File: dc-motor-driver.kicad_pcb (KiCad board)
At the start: 2 copper layers, 33 x 39.5 mm, 29 parts, among them J1 Conn_01x03, J10 Right, J11 RL, J12 RR, J2 MPU, J3 BAT, J4 Conn_01x03, J5 Power, J6 Left, J7 Conn_01x03, J8 FL, J9 FR, Q1 IRF7303, Q2 IRF7303

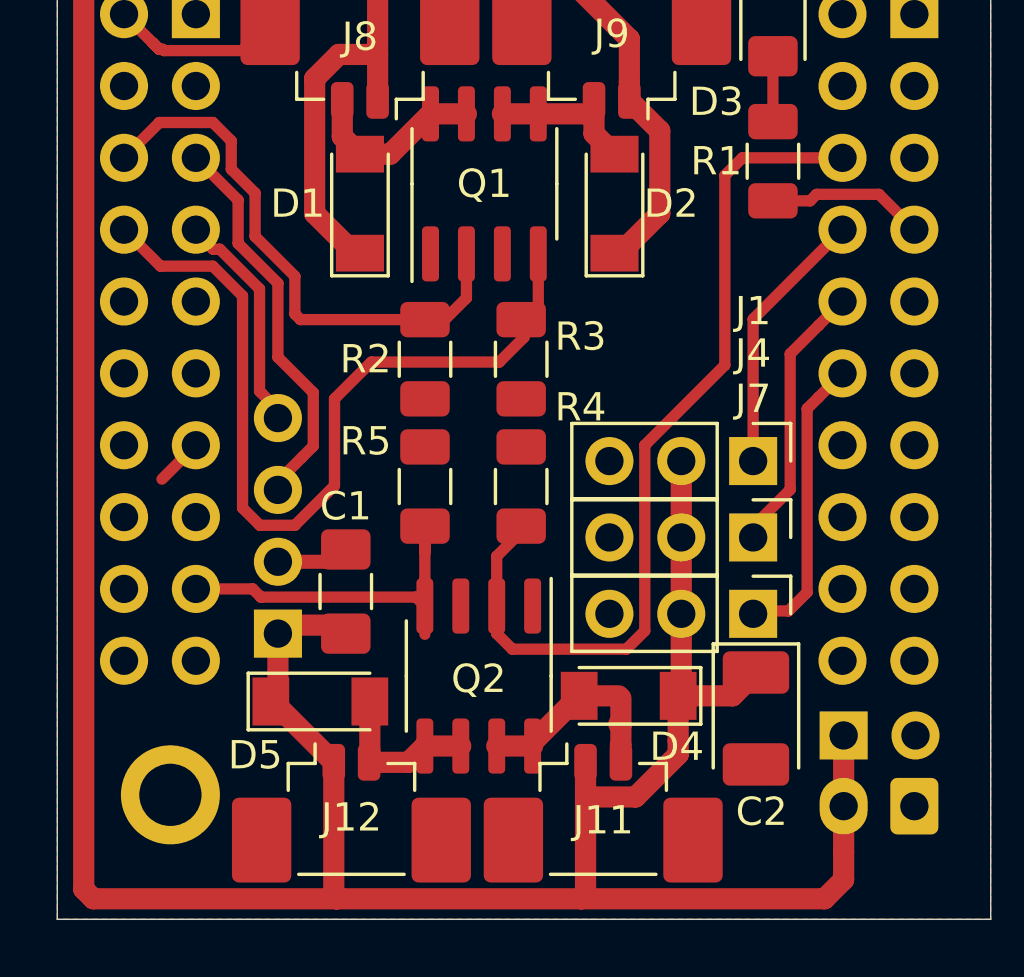
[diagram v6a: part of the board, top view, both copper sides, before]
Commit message: Aligned the pin headers some more.
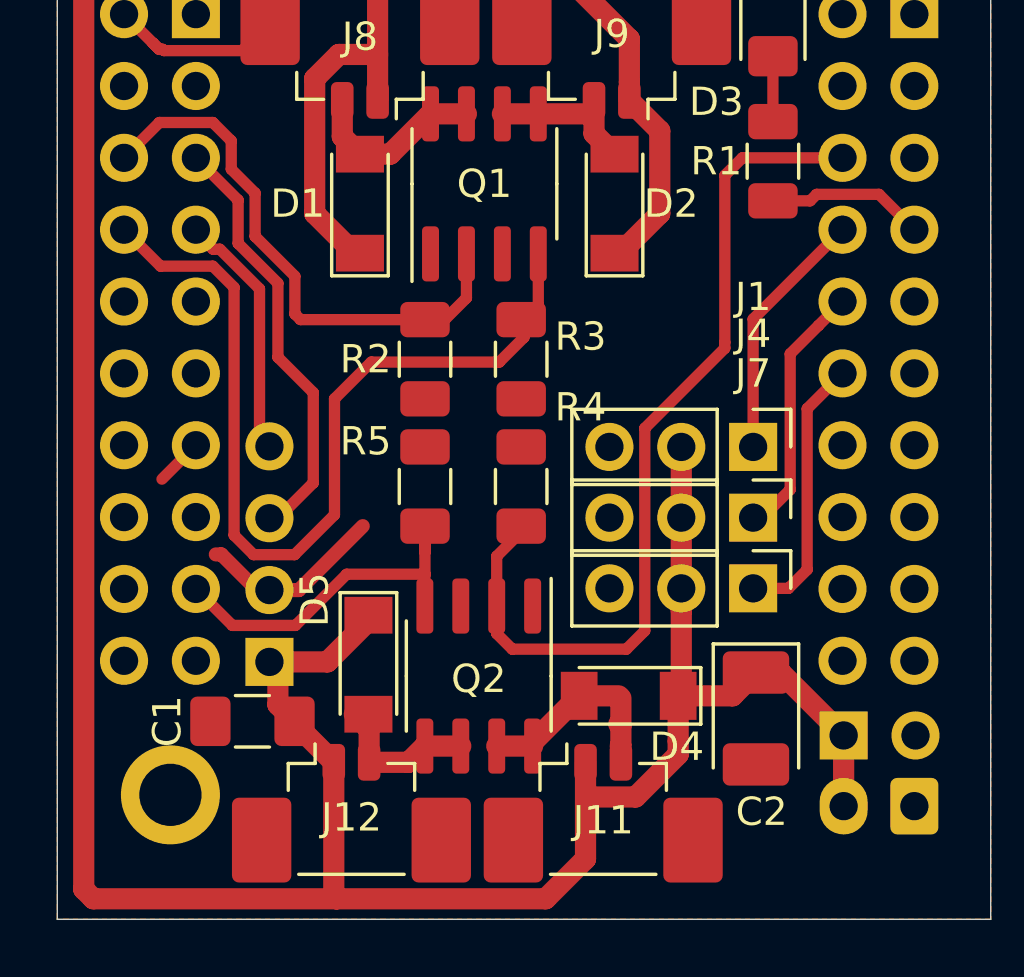
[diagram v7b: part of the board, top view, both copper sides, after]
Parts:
- moved C1 5.65 mm to (85.9, 142.5), turned to 180 degrees
- moved D5 2.14 mm to (90.0, 140.5), turned to 270 degrees
- moved J2 1.04 mm to (86.5, 140.4)
- moved J7 0.90 mm to (103.6, 137.8)
- moved J4 0.70 mm to (103.6, 135.3)
- moved J1 0.50 mm to (103.6, 132.8)
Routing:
- net VCC: track 144.5 -> 135.3 mm
- net GND: track 15.7 -> 19.5 mm
- net /FR: track 30.6 -> 32.8 mm
- net /RR: track 13.3 -> 11.6 mm
- net /SDA: track 7.70 -> 9.01 mm
- net /SCL: track 13.7 -> 15.0 mm
- net /ServoC: track 10.4 -> 9.64 mm
